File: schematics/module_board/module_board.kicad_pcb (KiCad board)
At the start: 2 copper layers, 30 x 30 mm, 26 parts, among them J1 Conn_01x04_Male, J10 Conn_01x02_Male, J2 Conn_01x10_Male, J5 Conn_01x06_Male, J9 Conn_01x02_Male, U1 RP2040, U2 W25Q16JVSSIQ, Y1 ABLS-12.000MHZ-B4-T

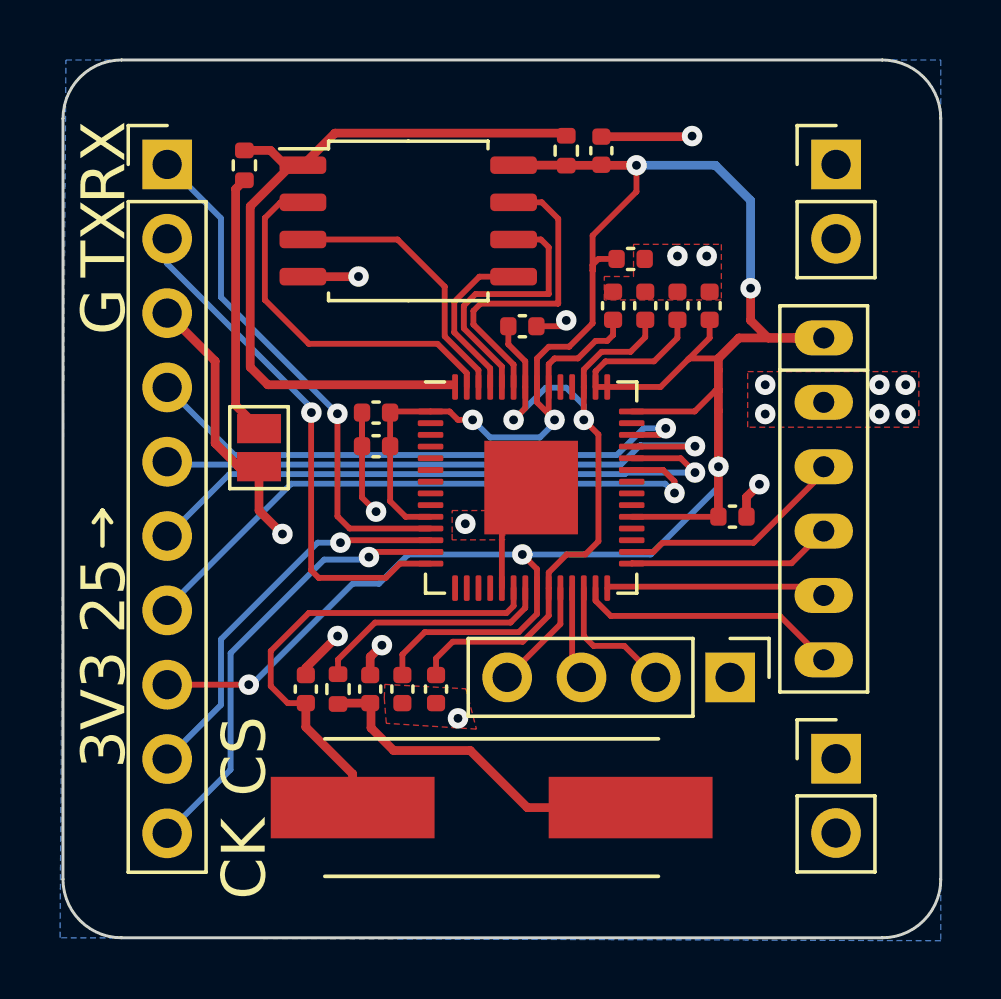
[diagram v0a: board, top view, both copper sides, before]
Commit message: Added LED to Module Board
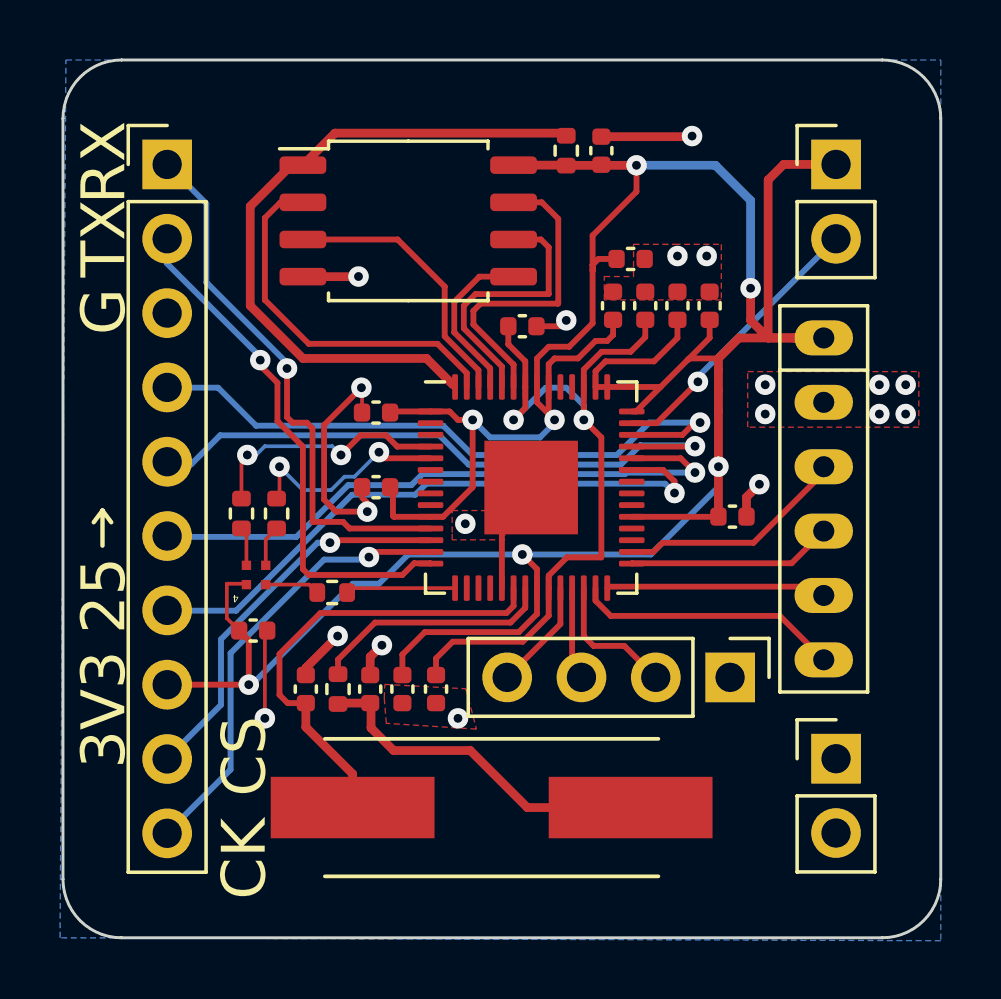
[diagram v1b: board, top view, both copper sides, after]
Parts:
- removed JP1: Jumper_2_Open, Jumper:SolderJumper-2_P1.3mm_Open_Pad1.0x1.5mm
- removed R1: 10k, Resistor_SMD:R_0402_1005Metric
- added C15: 100n, Capacitor_SMD:C_0402_1005Metric, F.Cu at (151.5, 94.5)
- added D1: LED_RGB, prototroller_footprints:LED_Cree-UHD111A, F.Cu at (151.6, 92.6)
- added R4: 1k, Resistor_SMD:R_0402_1005Metric, F.Cu at (151.1, 90.5)
- added R5: 1k, Resistor_SMD:R_0402_1005Metric, F.Cu at (152.3, 90.5)
- added R6: 1k, Resistor_SMD:R_0402_1005Metric, F.Cu at (154.2, 93.2)
- moved C10 1.40 mm to (155.7, 89.6)
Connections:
- J10 pad 1: unconnected-(J10-Pad1) -> +3V3
- J10 pad 2: unconnected-(J10-Pad2) -> /GPIO29_ADC3
- J9 pad 1: unconnected-(J9-Pad1) -> GND
- J9 pad 2: unconnected-(J9-Pad2) -> GND
- U1 pad 15: /GPIO12 -> /LED_B
- U1 pad 4: /GPIO2 -> /LED_R
- U1 pad 5: /GPIO3 -> /LED_G
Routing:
- net +3V3: track 100.3 -> 112.6 mm
- net /GPIO29_ADC3: track 0.00 -> 9.69 mm, vias 0 -> 1
- net /BOOTSEL_N: track 8.95 -> 0.00 mm
- net /LED_R: track 0.00 -> 8.52 mm, vias 0 -> 2
- net /LED_G: track 0.00 -> 7.25 mm, vias 0 -> 2
- net GND: track 28.5 -> 24.7 mm, vias 18 -> 19
- net /LED_B: track 0.00 -> 3.75 mm
- net /QSPI_NSS: track 26.8 -> 23.9 mm
- net /GPIO28_ADC2: track 19.6 -> 22.1 mm
- net /LB: track 0.00 -> 1.87 mm
- net /LG: track 0.00 -> 1.41 mm
- net /LR: track 0.00 -> 1.33 mm
- net /SPI1_RX: track 17.8 -> 18.7 mm
- net /GPIO27_ADC1: track 20.5 -> 21.4 mm

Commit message: master board rev b touchups
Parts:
- J1: value Conn_01x04_Male -> Conn_01x03_Male; footprint Connector_PinHeader_2.54mm:PinHeader_1x04_P2.54mm_Vertical -> Connector_PinHeader_2.54mm:PinHeader_1x03_P2.54mm_Vertical
- moved J1 1.88 mm to (165.9, 96.1)
- moved C2 0.65 mm to (158.4, 96.5)
- moved C12 0.50 mm to (157.1, 96.5)
- moved C9 0.30 mm to (155.8, 96.5)
- moved C8 0.10 mm to (153.2, 96.5)
- moved R3 0.10 mm to (154.5, 96.5)
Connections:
- J1 pad 1: GND -> /RESET_N
- J1 pad 2: /RESET_N -> /SWDIO
- J1 pad 3: /SWDIO -> /SWCLK
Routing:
- net +1V1: track 25.5 -> 24.6 mm
- net /SPI1_RX: track 18.7 -> 18.0 mm
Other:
- board text added: "28"
- board text added: "3V"
- board text added: "Ck"
- board text added: "Cs"
- board text added: "MOD BOARD REV B"
- board text added: "RS"
- board text added: "Rx"
- board text added: "Tx"
- board text removed: "3V3"
- board text removed: "CS"
- board text removed: "GN"
- board text removed: "MOD BOARD REV A"
- board text removed: "RES"
- board text removed: "RX"
- board text removed: "TX"

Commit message: add gerbers
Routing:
- net GND: track 24.9 -> 23.1 mm
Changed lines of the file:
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@@
       (effects (font (size 1 1) (thickness 0.15)))
     )
-    (fp_text user "4" (at 0.7 -0.8 180 unlocked) (layer "F.SilkS")
+    (fp_text user "4" (at 0.33 -0.85 unlocked) (layer "F.SilkS")
       (effects (font (size 0.25 0.25) (thickness 0.05)))
     )
@@
   (segment (start 151.27 91.18) (end 151.27 92.27) (width 0.127) (layer "F.Cu") (net 6))
   (segment (start 154.387352 94.687352) (end 153.2 95.874704) (width 0.3) (layer "F.Cu") (net 13))
-  (segment (start 166.48 77.62) (end 163.4 77.62) (width 0.3) (layer "F.Cu") (net 13))
   (segment (start 168.36 90.60625) (end 168.36 89.94) (width 0.3) (layer "F.Cu") (net 13))
   (segment (start 154.336 90.436) (end 153.923 90.023) (width 0.2) (layer "F.Cu") (net 13))
@@
   (segment (start 155.4 90.436) (end 155.22 90.256) (width 0.2) (layer "F.Cu") (net 13))
   (segment (start 155.4 90.436) (end 154.336 90.436) (width 0.2) (layer "F.Cu") (net 13))
+  (segment (start 163.41 77.62) (end 163.4 77.62) (width 0.3) (layer "F.Cu") (net 13))
   (segment (start 160.40625 90.20625) (end 161 89.6125) (width 0.2) (layer "F.Cu") (net 13))
   (segment (start 160 93.05) (end 160 90.6125) (width 0.2) (layer "F.Cu") (net 13))
   (segment (start 155.22 90.256) (end 155.22 89.6) (width 0.2) (layer "F.Cu") (net 13))
   (segment (start 155.8 96.02) (end 155.8 95.1) (width 0.3) (layer "F.Cu") (net 13))
+  (segment (start 164.28 76.75) (end 163.41 77.62) (width 0.3) (layer "F.Cu") (net 13))
   (segment (start 162 84.1) (end 162.2 83.9) (width 0.2) (layer "F.Cu") (net 13))
   (segment (start 168.36 89.94) (end 168.8 89.5) (width 0.3) (layer "F.Cu") (net 13))
@@
   (segment (start 155.22 86.22) (end 155.2 86.2) (width 0.3) (layer "F.Cu") (net 13))
   (segment (start 153.923 87.477) (end 155.2 86.2) (width 0.2) (layer "F.Cu") (net 13))
-  (segment (start 166.5 77.6) (end 166.48 77.62) (width 0.3) (layer "F.Cu") (net 13))
   (segment (start 155.8 95.1) (end 155.9 95) (width 0.3) (layer "F.Cu") (net 13))
   (via (at 169 87.1) (size 0.7) (drill 0.3) (layers "F.Cu" "B.Cu") (free) (net 13))
@@
   (via (at 158.89 91.09) (size 0.7) (drill 0.3) (layers "F.Cu" "B.Cu") (free) (net 13))
   (via (at 166 81.7) (size 0.7) (drill 0.3) (layers "F.Cu" "B.Cu") (free) (net 13))
-  (via (at 166.5 77.6) (size 0.7) (drill 0.3) (layers "F.Cu" "B.Cu") (net 13))
+  (via (at 164.28 76.75) (size 0.7) (drill 0.3) (layers "F.Cu" "B.Cu") (net 13))
   (via (at 167 81.7) (size 0.7) (drill 0.3) (layers "F.Cu" "B.Cu") (free) (net 13))
   (via (at 155.4 90.436) (size 0.7) (drill 0.3) (layers "F.Cu" "B.Cu") (net 13))
@@
   (segment (start 151.9 83.2) (end 153.4 84.7) (width 0.2) (layer "F.Cu") (net 40))
   (segment (start 153.2 78.595) (end 152.595 78.595) (width 0.3) (layer "F.Cu") (net 41))
+  (segment (start 162.11 77.5) (end 154.295 77.5) (width 0.3) (layer "F.Cu") (net 41))
+  (segment (start 162.2 77.59) (end 162.11 77.5) (width 0.3) (layer "F.Cu") (net 41))
   (segment (start 153.2 85.2) (end 151.4 83.4) (width 0.3) (layer "F.Cu") (net 41))
-  (segment (start 154.295 77.5) (end 153.2 78.595) (width 0.3) (layer "F.Cu") (net 41))
   (segment (start 157.425 85.2) (end 153.2 85.2) (width 0.3) (layer "F.Cu") (net 41))
   (segment (start 158.325 86.1) (end 157.425 85.2) (width 0.3) (layer "F.Cu") (net 41))
+  (segment (start 154.295 77.5) (end 153.2 78.595) (width 0.3) (layer "F.Cu") (net 41))
   (segment (start 151.4 80) (end 152.805 78.595) (width 0.3) (layer "F.Cu") (net 41))
   (segment (start 151.4 83.4) (end 151.4 80) (width 0.3) (layer "F.Cu") (net 41))
-  (segment (start 162.11 77.5) (end 154.295 77.5) (width 0.3) (layer "F.Cu") (net 41))
-  (segment (start 162.2 77.59) (end 162.11 77.5) (width 0.3) (layer "F.Cu") (net 41))
   (segment (start 152.805 78.595) (end 153.2 78.595) (width 0.3) (layer "F.Cu") (net 41))
   (segment (start 164.4 100.55) (end 160.87 100.55) (width 0.3) (layer "F.Cu") (net 42))
@@
   (segment (start 163.2 93.479237) (end 163.720763 94) (width 0.2) (layer "F.Cu") (net 46))
   (segment (start 163.720763 94) (end 169.5 94) (width 0.2) (layer "F.Cu") (net 46))
-  (segment (start 168.6 91.5) (end 171 89.1) (width 0.2) (layer "F.Cu") (net 47))
+  (segment (start 164.866737 91.8125) (end 165.309237 91.37) (width 0.2) (layer "F.Cu") (net 47))
   (segment (start 171 89.1) (end 171 88.9) (width 0.2) (layer "F.Cu") (net 47))
-  (segment (start 165.177118 91.8125) (end 165.489618 91.5) (width 0.2) (layer "F.Cu") (net 47))
-  (segment (start 165.489618 91.5) (end 168.6 91.5) (width 0.2) (layer "F.Cu") (net 47))
-  (segment (start 164.4375 91.8125) (end 165.177118 91.8125) (width 0.2) (layer "F.Cu") (net 47))
+  (segment (start 165.309237 91.37) (end 168.73 91.37) (width 0.2) (layer "F.Cu") (net 47))
+  (segment (start 164.4375 91.8125) (end 164.866737 91.8125) (width 0.2) (layer "F.Cu") (net 47))
+  (segment (start 168.73 91.37) (end 171 89.1) (width 0.2) (layer "F.Cu") (net 47))
   (segment (start 157.5625 88.6125) (end 156.009 88.6125) (width 0.2) (layer "F.Cu") (net 48))
   (segment (start 152.4 88.9) (end 152.4 89.89) (width 0.127) (layer "F.Cu") (net 48))
@@
         (xy 163.5 83.2)
         (xy 163.5 82.4)
-        (xy 164.5 82.4)
-        (xy 164.5 81.3)
+        (xy 164.3 82.4)
+        (xy 164.3 81.2)
       )
     )
